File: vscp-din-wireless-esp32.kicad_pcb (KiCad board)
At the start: 2 copper layers, 64.8 x 51 mm, 18 parts, among them J1 Conn_Left_I2C, J2 Conn_Right_Power, J3 Conn_01x06, U1 ESP32-WROOM-32D

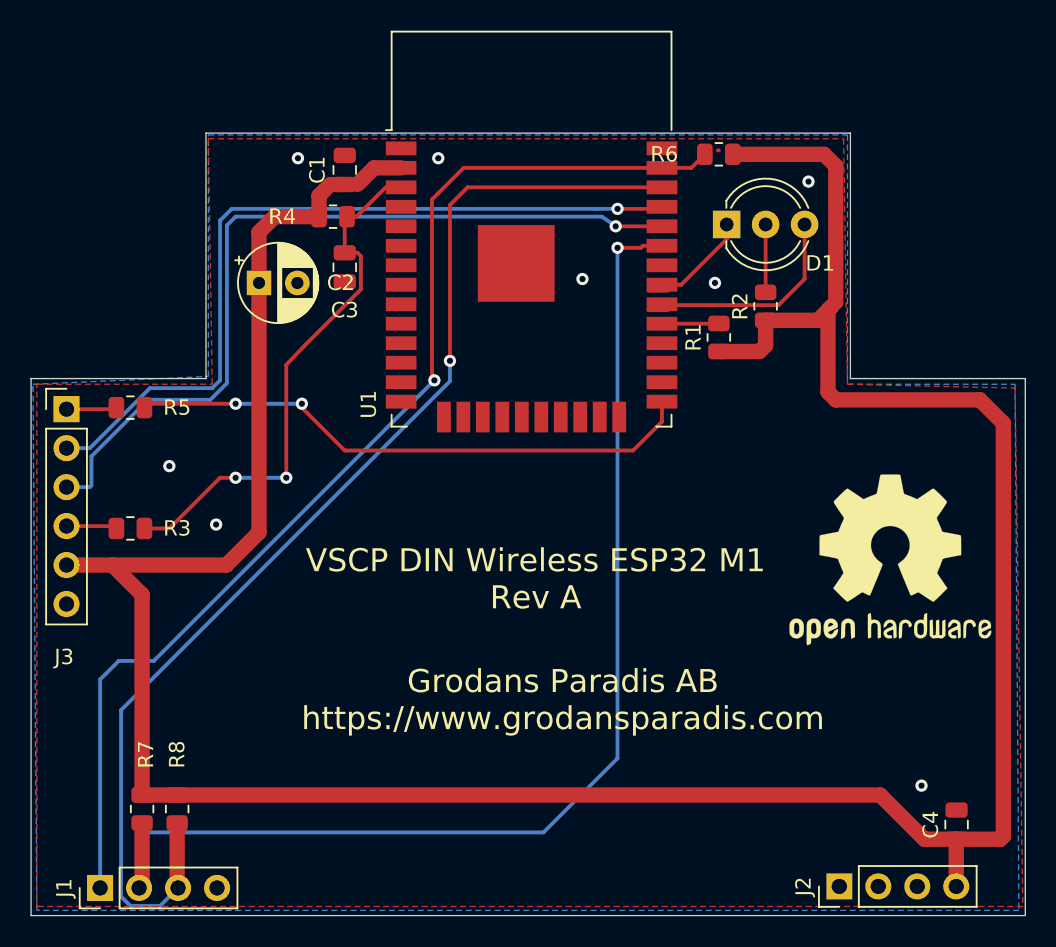
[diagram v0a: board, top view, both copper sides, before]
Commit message: Fixed board to board connector
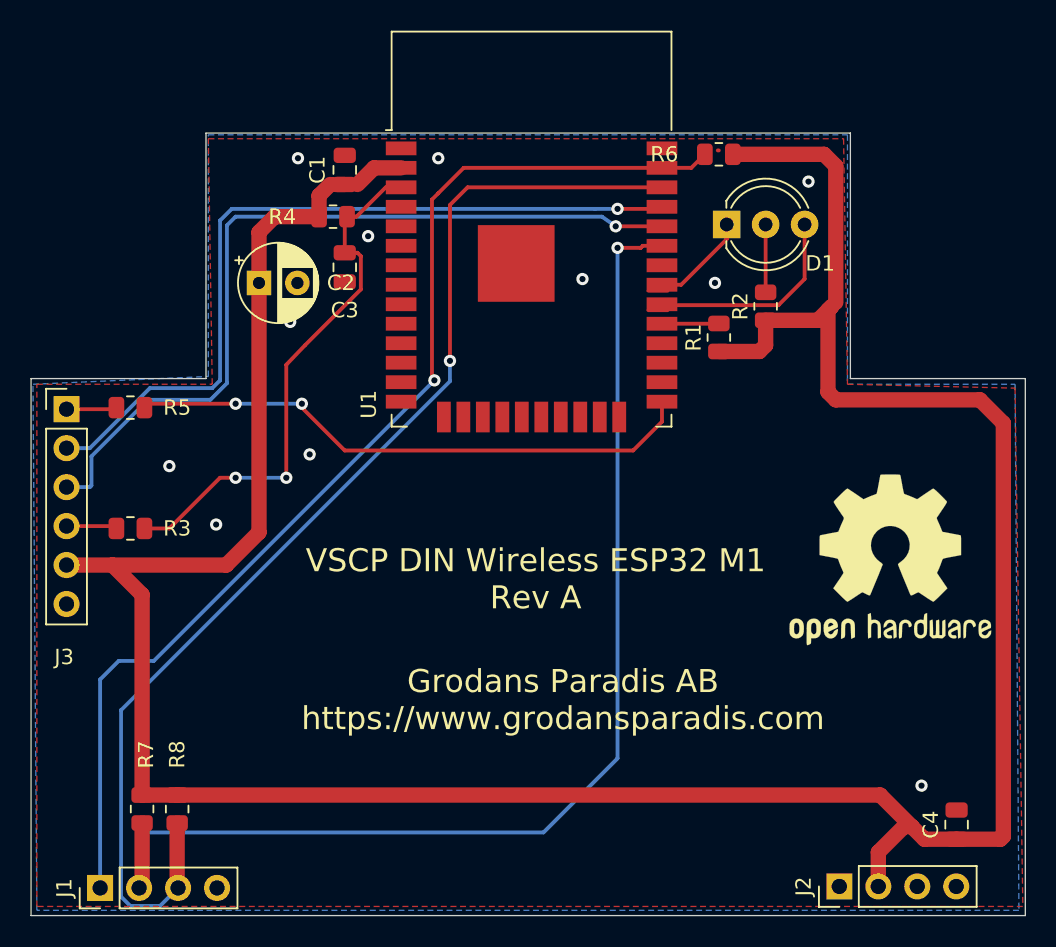
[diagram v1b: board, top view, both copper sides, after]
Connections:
- J2 pad 2: Net-(J2-Pad2) -> VCC
- J2 pad 4: VCC -> Net-(J2-Pad4)
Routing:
- net VCC: track 191.8 -> 193.8 mm
- net GND: vias 8 -> 11
